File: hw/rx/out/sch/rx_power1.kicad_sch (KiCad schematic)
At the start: 16 parts, among them J1 backplane 2x13, U4 TLV76733, U5 TLV76733

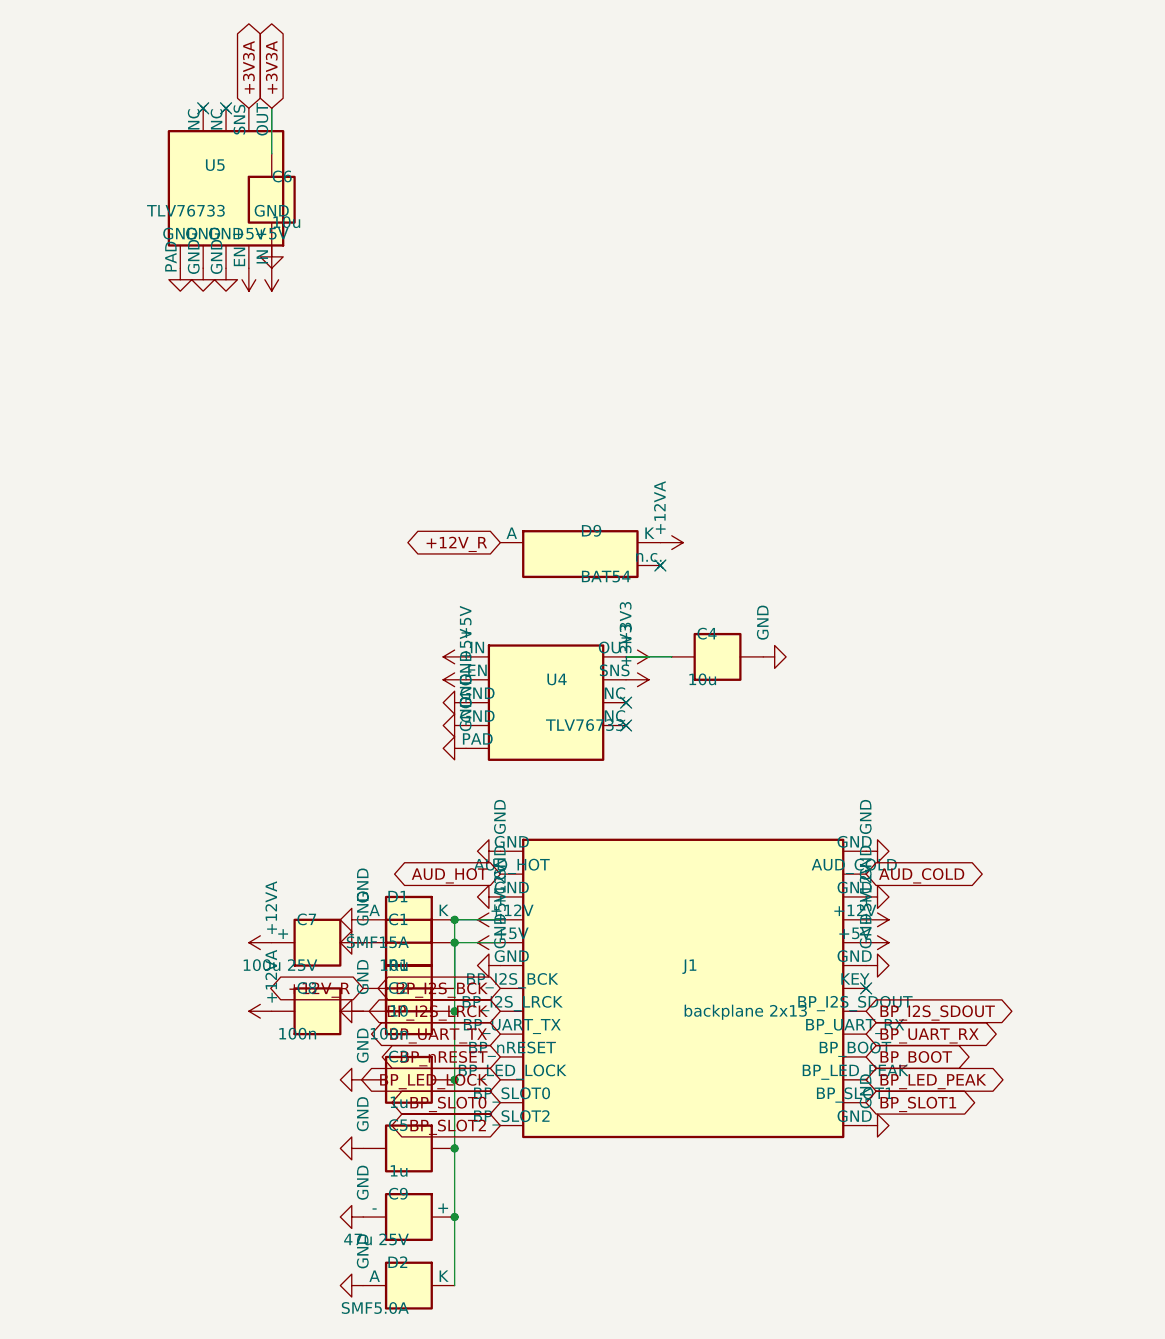
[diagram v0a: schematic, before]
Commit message: hw/rx: BT40E + TQ2SA footprints, THT underside backplane header, bring-up test points (#34)
Co-Authored-By: Claude Opus 5.5 <noreply@anthropic.com>
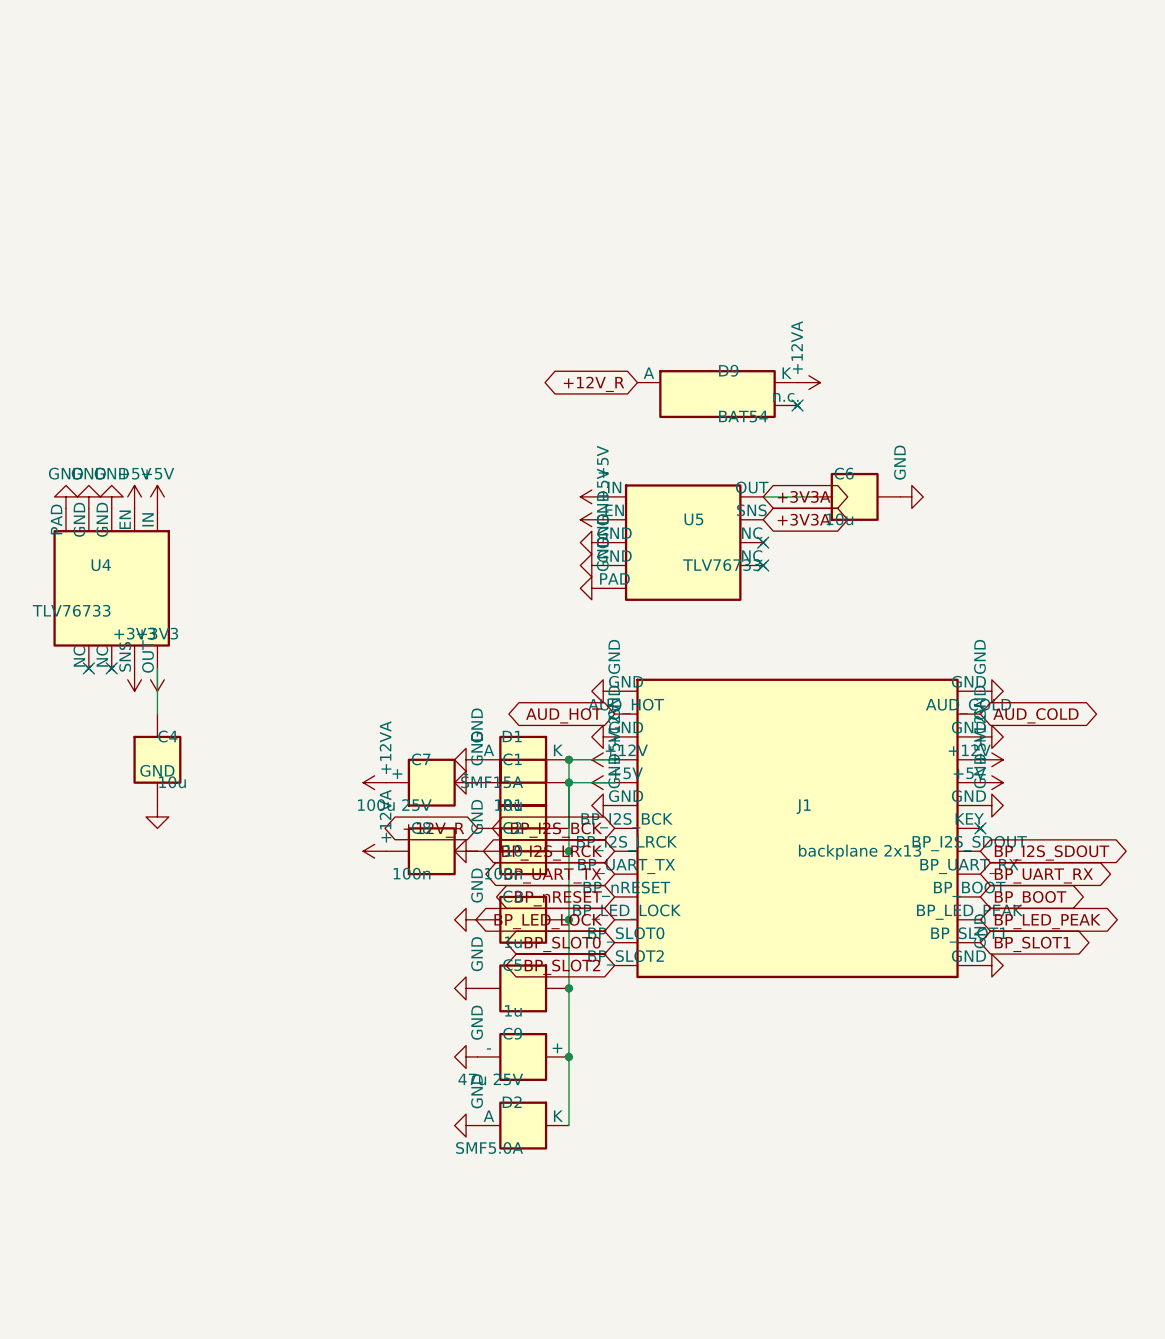
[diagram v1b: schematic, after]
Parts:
- J1: footprint Connector_PinHeader_2.54mm:PinHeader_2x13_P2.54mm_Vertical_SMD -> Connector_PinHeader_2.54mm:PinHeader_2x13_P2.54mm_Vertical; MPN HDR_2x13_2.54_SMD_KEY14 -> HDR_2x13_2.54_KEY14
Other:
- moved on the sheet: C1, C2, C3, C4, C5, C6, C7, C8, C9, D1, D2, D9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
